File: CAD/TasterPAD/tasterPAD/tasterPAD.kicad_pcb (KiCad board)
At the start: 2 copper layers, 28 parts, among them J1 Conn_01x04_Pin, J2 Conn_01x17_Pin, J3 SPI Programmer IF, U1 74HC165, U2 74HC165, U3 ATtiny13A-P

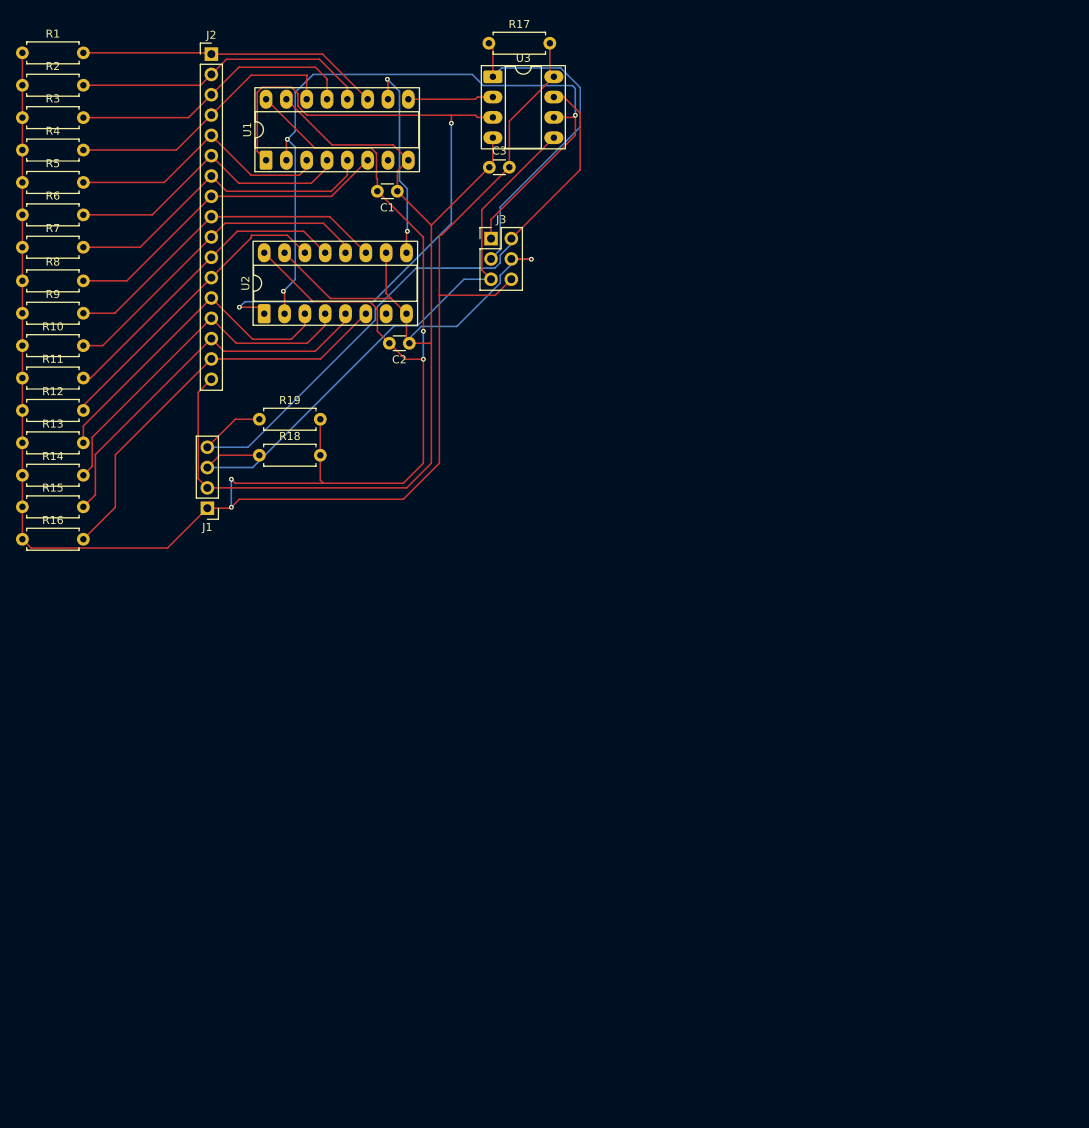
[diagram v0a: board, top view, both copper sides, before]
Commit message: updated Taster PCB
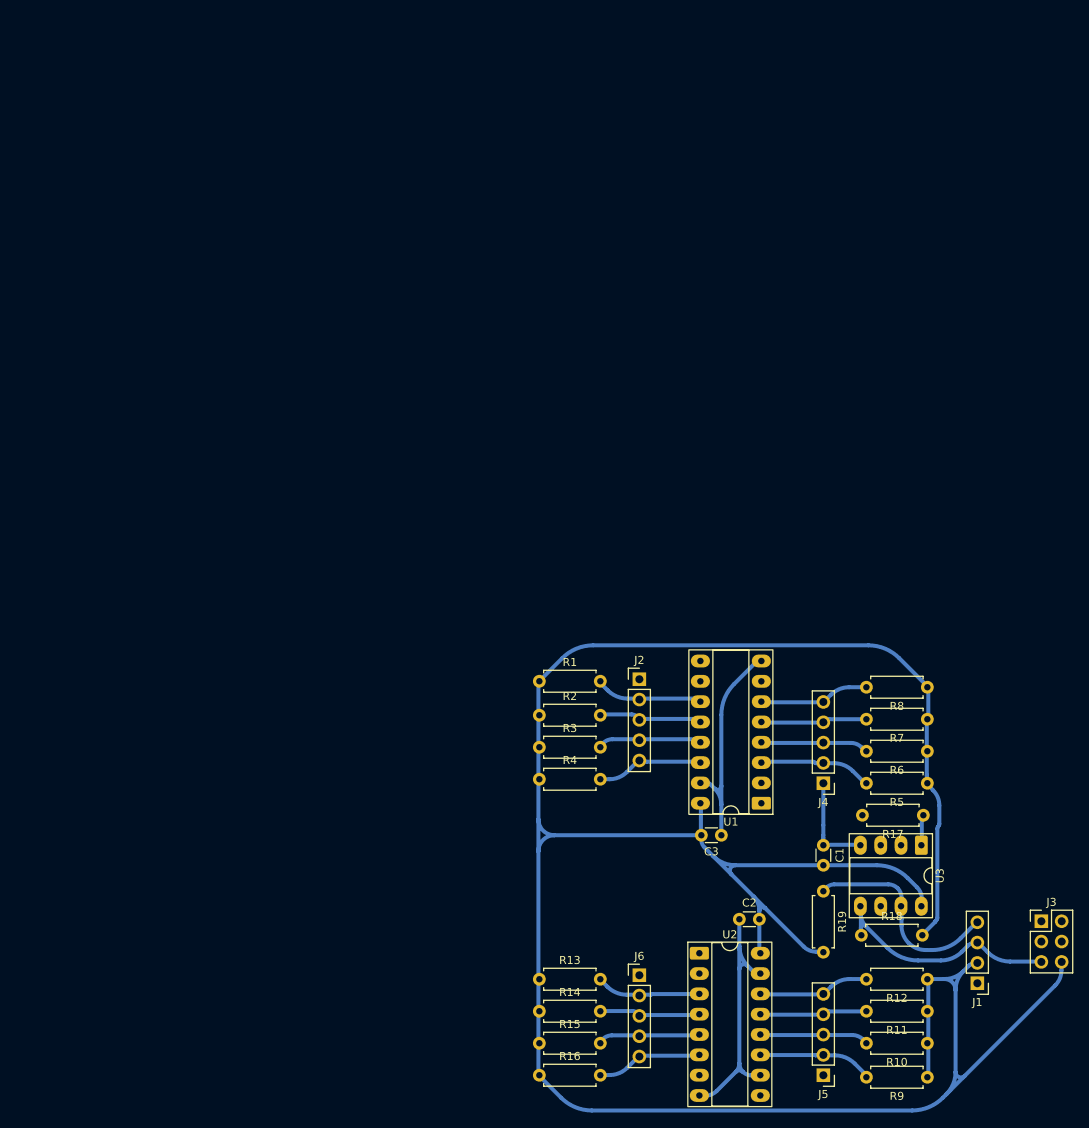
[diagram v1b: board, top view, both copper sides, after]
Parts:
- added J4: Conn_01x05_Pin, Connector_PinHeader_2.54mm:PinHeader_1x05_P2.54mm_Vertical, F.Cu at (127.0, 114.0)
- added J5: Conn_01x05_Pin, Connector_PinHeader_2.54mm:PinHeader_1x05_P2.54mm_Vertical, F.Cu at (127.0, 150.5)
- added J6: Conn_01x05_Pin, Connector_PinHeader_2.54mm:PinHeader_1x05_P2.54mm_Vertical, F.Cu at (104.0, 138.0)
- J2: value Conn_01x17_Pin -> Conn_01x05_Pin; footprint Connector_PinHeader_2.54mm:PinHeader_1x17_P2.54mm_Vertical -> Connector_PinHeader_2.54mm:PinHeader_1x05_P2.54mm_Vertical
- moved R9 148.0 mm to (140.0, 150.8), turned to 180 degrees
- moved R10 142.8 mm to (140.0, 146.5), turned to 180 degrees
- moved R11 138.1 mm to (140.0, 142.5), turned to 180 degrees
- moved R5 135.8 mm to (140.0, 114.0), turned to 180 degrees
- moved R12 133.6 mm to (140.0, 138.5), turned to 180 degrees
- moved R6 131.5 mm to (140.0, 110.0), turned to 180 degrees
- moved R7 127.6 mm to (140.0, 106.0), turned to 180 degrees
- moved R8 124.0 mm to (140.0, 102.0), turned to 180 degrees
- moved J1 113.1 mm to (146.2, 139.0)
- moved R17 110.7 mm to (139.5, 118.0), turned to 180 degrees
- moved U3 110.0 mm to (139.2, 121.8), turned to -90 degrees
- moved J3 109.6 mm to (154.2, 131.2)
- moved R2 101.9 mm to (91.5, 105.5)
- moved R3 101.8 mm to (91.5, 109.5)
- moved R4 101.8 mm to (91.5, 113.5)
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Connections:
- J1 pad 1: VCC -> GND
- J1 pad 2: GND -> VCC
- J2 pad 1: /IN01 -> GND
- J2 pad 2: /IN02 -> /IN01
- J2 pad 3: /IN03 -> /IN02
- J2 pad 4: /IN04 -> /IN03
- J2 pad 5: /IN05 -> /IN04
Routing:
- net /CLK: track 94.4 -> 0.00 mm, vias 3 -> 0
- net GND: track 170.7 -> 76.9 mm, vias 1 -> 0
- net /PL: track 88.9 -> 0.00 mm, vias 2 -> 0
- net /SDA: track 81.9 -> 26.8 mm
- net /SCL: track 74.2 -> 31.0 mm
- net /RESET: track 42.8 -> 3.90 mm
- net /IN16: track 50.8 -> 13.3 mm
- net /IN15: track 47.6 -> 12.7 mm
- net /IN14: track 44.2 -> 12.5 mm
- net VCC: track 308.1 -> 337.0 mm, vias 4 -> 0
- net /IN08: track 41.8 -> 13.9 mm
- net /IN09: track 42.2 -> 14.4 mm
- net /IN13: track 40.8 -> 13.1 mm
- net /IN10: track 41.2 -> 13.9 mm
- net /IN07: track 40.2 -> 13.2 mm
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
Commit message: Final PcB
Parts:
- added B1: PinHeader_1x02_P2.54mm_Vertical, Connector_PinHeader_2.54mm:PinHeader_1x02_P2.54mm_Vertical, F.Cu at (103.0, 77.5)
- added B2: PinHeader_1x02_P2.54mm_Vertical, Connector_PinHeader_2.54mm:PinHeader_1x02_P2.54mm_Vertical, F.Cu at (74.8, 88.0)
- added B3: PinHeader_1x02_P2.54mm_Vertical, Connector_PinHeader_2.54mm:PinHeader_1x02_P2.54mm_Vertical, F.Cu at (97.8, 69.5)
- added B4: PinHeader_1x02_P2.54mm_Vertical, Connector_PinHeader_2.54mm:PinHeader_1x02_P2.54mm_Vertical, F.Cu at (135.8, 78.0)
- added B5: PinHeader_1x02_P2.54mm_Vertical, Connector_PinHeader_2.54mm:PinHeader_1x02_P2.54mm_Vertical, F.Cu at (70.8, 62.8)
- added B5: PinHeader_1x02_P2.54mm_Vertical, Connector_PinHeader_2.54mm:PinHeader_1x02_P2.54mm_Vertical, F.Cu at (107.2, 88.0)
- added B6: PinHeader_1x02_P2.54mm_Vertical, Connector_PinHeader_2.54mm:PinHeader_1x02_P2.54mm_Vertical, F.Cu at (130.5, 69.5)
- added MH1: MountingHole_3.2mm_M3, MountingHole:MountingHole_3.2mm_M3, F.Cu at (49.0, 57.0)
- added MH2: MountingHole_3.2mm_M3, MountingHole:MountingHole_3.2mm_M3, F.Cu at (134.2, 57.0)
- added MH3: MountingHole_3.2mm_M3, MountingHole:MountingHole_3.2mm_M3, F.Cu at (49.2, 99.5)
- added MH4: MountingHole_3.2mm_M3, MountingHole:MountingHole_3.2mm_M3, F.Cu at (134.0, 99.5)
- added SB1: PinHeader_1x02_P2.54mm_Vertical, Connector_PinHeader_2.54mm:PinHeader_1x02_P2.54mm_Vertical, F.Cu at (103.2, 69.5)
- added SB2: PinHeader_1x02_P2.54mm_Vertical, Connector_PinHeader_2.54mm:PinHeader_1x02_P2.54mm_Vertical, F.Cu at (69.0, 88.0)
- added SB3: PinHeader_1x02_P2.54mm_Vertical, Connector_PinHeader_2.54mm:PinHeader_1x02_P2.54mm_Vertical, F.Cu at (135.8, 69.5)
- added SB4: PinHeader_1x02_P2.54mm_Vertical, Connector_PinHeader_2.54mm:PinHeader_1x02_P2.54mm_Vertical, F.Cu at (101.5, 88.0)
- added SB5: PinHeader_1x02_P2.54mm_Vertical, Connector_PinHeader_2.54mm:PinHeader_1x02_P2.54mm_Vertical, F.Cu at (49.0, 70.0)
- added SB6: PinHeader_1x02_P2.54mm_Vertical, Connector_PinHeader_2.54mm:PinHeader_1x02_P2.54mm_Vertical, F.Cu at (68.0, 74.2)
- added SB7: PinHeader_1x01_P2.54mm_Vertical, Connector_PinHeader_2.54mm:PinHeader_1x01_P2.54mm_Vertical, F.Cu at (65.0, 62.8)
- moved J1 109.3 mm to (53.0, 82.0), turned to 90 degrees
- moved R17 108.7 mm to (45.0, 64.2), turned to -90 degrees
- moved J3 105.8 mm to (68.0, 70.0), turned to 90 degrees
- moved U3 103.5 mm to (52.8, 65.0), turned to 0 degrees
- moved R16 96.5 mm to (113.5, 56.5), turned to -90 degrees
- moved R15 93.7 mm to (117.5, 56.5), turned to -90 degrees
- moved R14 91.0 mm to (121.2, 56.5), turned to -90 degrees
- moved R13 88.7 mm to (125.2, 56.5), turned to -90 degrees
- moved R18 87.5 mm to (57.8, 86.2), turned to -90 degrees
- moved R19 77.8 mm to (61.0, 86.2)
- moved C3 76.2 mm to (52.2, 76.2), turned to 0 degrees
- moved R8 75.3 mm to (80.0, 56.5), turned to -90 degrees
- moved R5 75.1 mm to (91.8, 56.5), turned to -90 degrees
- moved R7 74.9 mm to (83.8, 56.5), turned to -90 degrees
- moved R6 74.8 mm to (87.8, 56.5), turned to -90 degrees
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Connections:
- J1 pad 3: /SCL -> /SDA
- J1 pad 4: /SDA -> /SCL
- R18 pad 1: /SCL -> /SDA
- R19 pad 1: /SDA -> /SCL
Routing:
- net GND: track 76.9 -> 213.0 mm
- net VCC: track 337.0 -> 285.5 mm
- net /CLK: track 0.00 -> 43.4 mm
- net /CASCADE: track 0.00 -> 28.3 mm
- net /PL: track 0.00 -> 27.1 mm
- net /RESET: track 3.90 -> 26.3 mm
- net /Q7: track 0.00 -> 14.4 mm
- net /IN10: track 13.9 -> 11.4 mm
- net /IN09: track 14.4 -> 12.1 mm
- net /IN11: track 13.6 -> 11.3 mm
- net /IN06: track 13.4 -> 11.1 mm
- net /IN12: track 14.2 -> 11.9 mm
- net /IN05: track 14.0 -> 11.7 mm
- net /IN04: track 13.6 -> 11.4 mm
- net /IN03: track 13.1 -> 10.9 mm
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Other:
- board outline added: 100 x 53.8 mm
- board text added: "J4"
